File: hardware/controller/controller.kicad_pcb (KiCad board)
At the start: 4 copper layers, 100 x 70 mm, 192 parts, among them J1 USB_C_Receptacle_USB2.0_14P, J10 Conn_01x01, J11 Conn_01x01, J12 Conn_02x03_Odd_Even, J2 IDC-10, J3 XT-60, J4 Conn_01x07, J5 Conn_01x01, J6 Conn_01x01, J7 Conn_01x01, J8 Conn_02x03_Odd_Even, J9 Conn_01x01, Q1 SUD50P04-08, Q10 AOD66406, Q11 AOD66406, Q12 AOD66406, Q13 AOD66406, Q2 AOD66406, Q3 AOD66406, Q4 AOD66406, Q5 AOD66406, Q6 AOD66406, Q7 AOD66406, Q8 AOD66406, Q9 AOD66406, SW1 SW_Push, SW2 SW_Push, SW3 SW_Push, SW4 SW_SPST, U1 USBLC6-2SC6, U10 LM2105D, U11 MCP6541, U12 LM2105D, U13 MCP6541, U14 LM2105D, U15 MCP6541, U16 LM2105D, U17 MCP6541, U18 LM2105D, U19 MCP6541, U2 ESP32-C3-WROOM-02, U3 STM32U535RET6, U4 nRF24L01+ 2.4Gz Mini SMD, U5 LM1117MP-3.3, U6 LV14340, U7 MPU-6050, U8 LM2105D, U9 MCP6541, Y1 8MHz

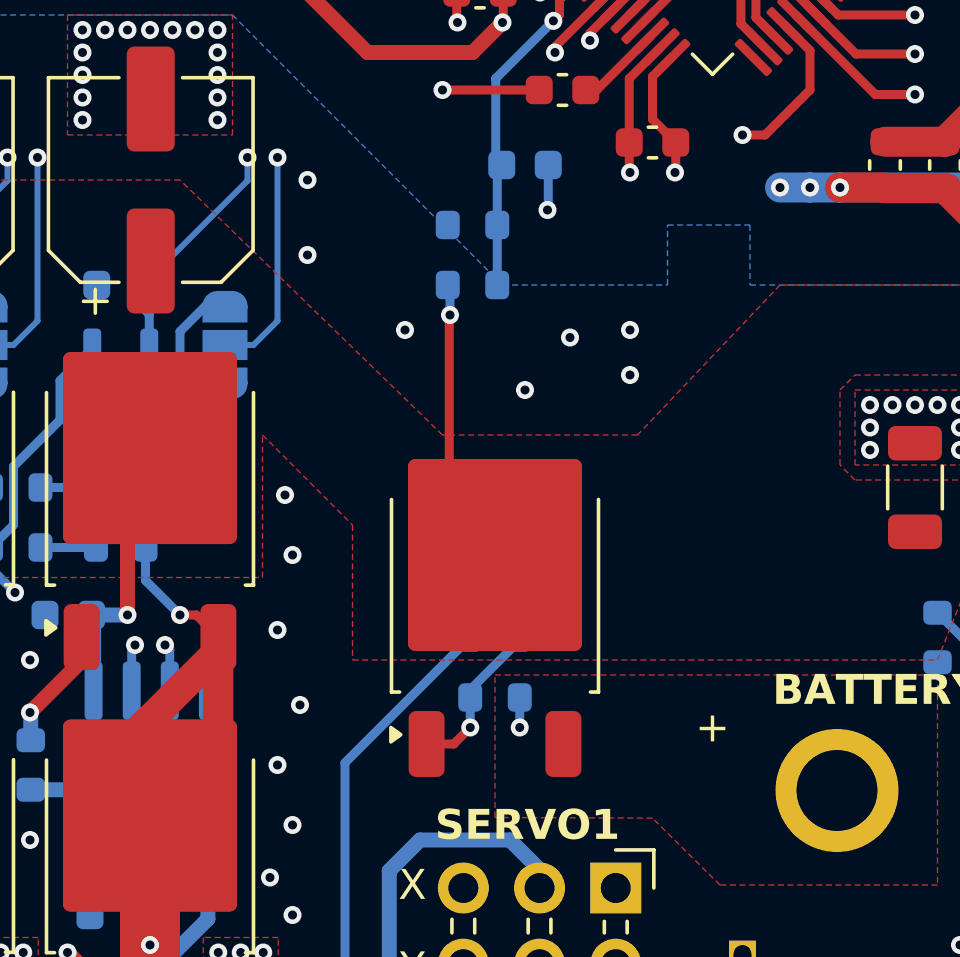
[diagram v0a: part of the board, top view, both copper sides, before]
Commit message: use diffrent P-MOSFET
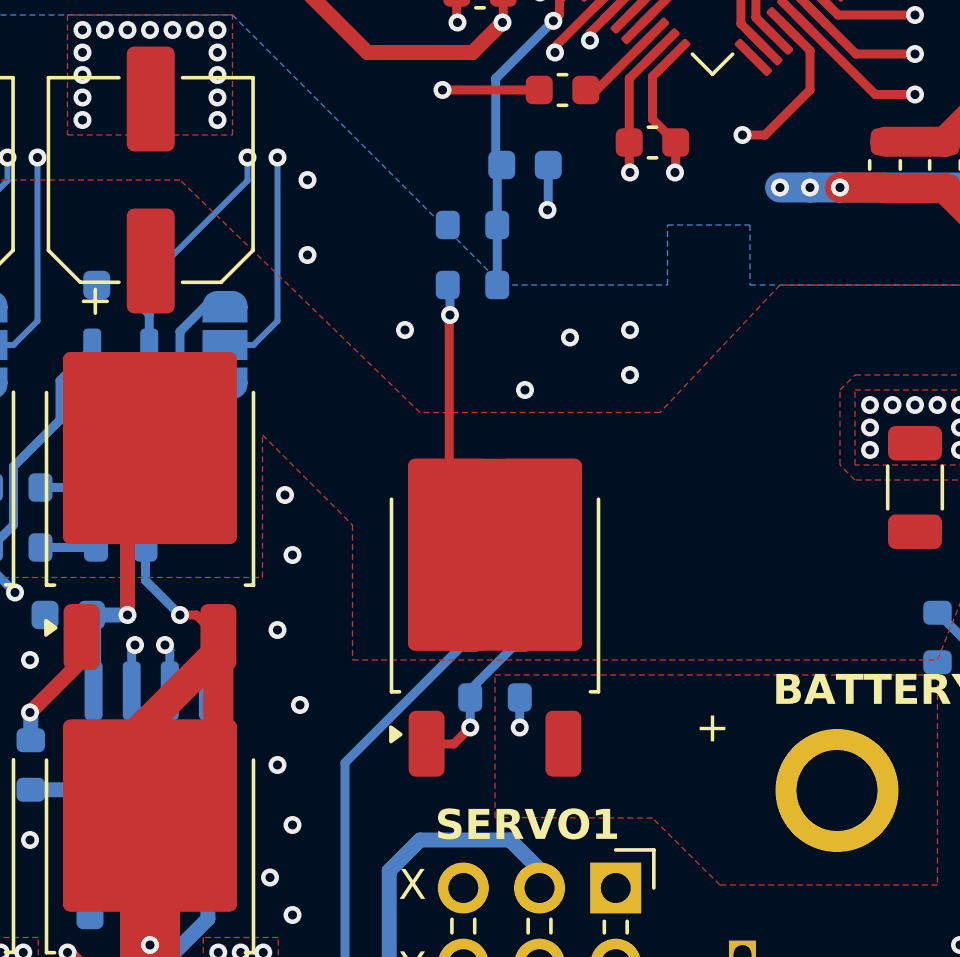
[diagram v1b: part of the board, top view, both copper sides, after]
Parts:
- Q1: value SUD50P04-08 -> AOD4189

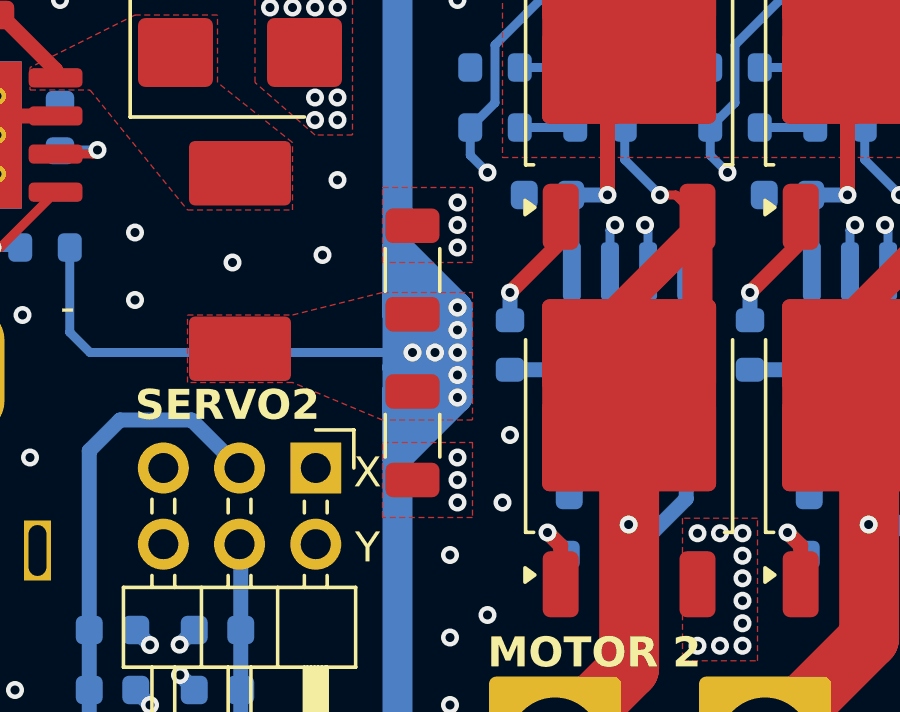
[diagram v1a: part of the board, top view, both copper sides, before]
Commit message: bigger capacitors on step down
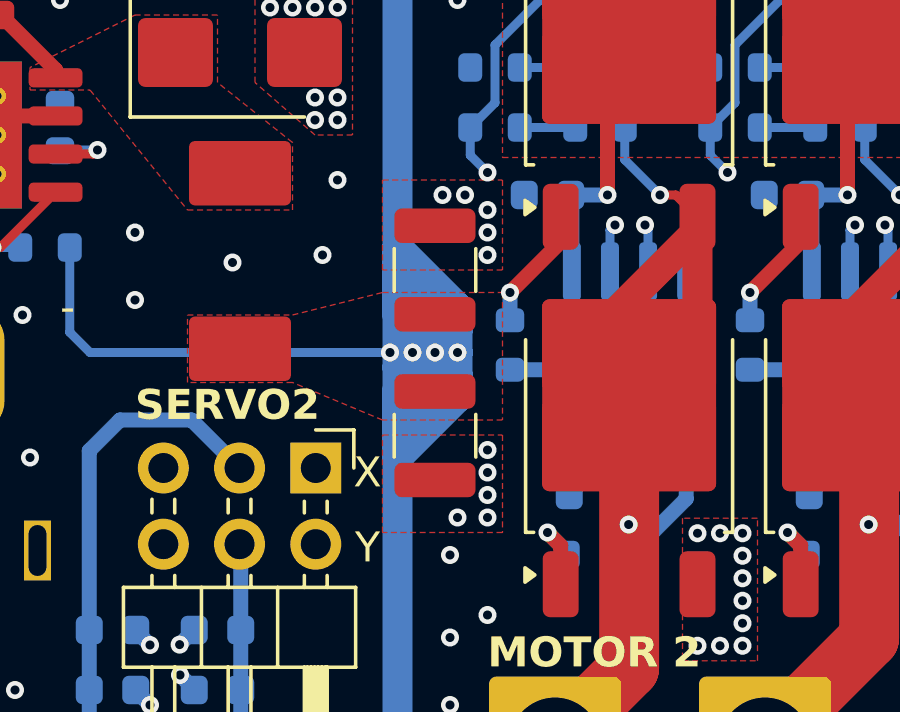
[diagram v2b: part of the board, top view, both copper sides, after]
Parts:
- C26, C27: footprint Capacitor_SMD:C_1206_3216Metric -> Capacitor_SMD:C_1210_3225Metric
- moved C26 0.75 mm to (170.0, 100.2)
- moved C27 0.75 mm to (170.0, 105.8)
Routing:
- net GND: vias 312 -> 314
- net +5V: vias 10 -> 7
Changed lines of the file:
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@@
 		)
 	)
-	(footprint "Capacitor_SMD:C_1206_3216Metric"
+	(footprint "Capacitor_SMD:C_1210_3225Metric"
 		(layer "F.Cu")
-		(at 169.25 105.775 -90)
-		(descr "Capacitor SMD 1206 (3216 Metric), square (rectangular) end terminal, IPC_7351 nominal, (Body size source: IPC-SM-782 page 76, https://www.pcb-3d.com/wordpress/wp-content/uploads/ipc-sm-782a_amendment_1_and_2.pdf), generated with kicad-footprint-generator")
+		(at 170 105.775 -90)
+		(descr "Capacitor SMD 1210 (3225 Metric), square (rectangular) end terminal, IPC_7351 nominal, (Body size source: IPC-SM-782 page 76, https://www.pcb-3d.com/wordpress/wp-content/uploads/ipc-sm-782a_amendment_1_and_2.pdf), generated with kicad-footprint-generator")
 		(tags "capacitor")
 		(property "Reference" "C27"
-			(at 0 -1.85 90)
+			(at 0 -2.3 270)
 			(layer "F.SilkS")
 			(hide yes)
@@
 		)
 		(property "Value" "47u/16V"
-			(at 0 1.85 90)
+			(at 0 2.3 -90)
 			(layer "F.Fab")
 			(effects
@@
 			)
 		)
-		(property "Footprint" "Capacitor_SMD:C_1206_3216Metric"
+		(property "Footprint" "Capacitor_SMD:C_1210_3225Metric"
 			(at 0 0 -90)
 			(unlocked yes)
@@
 		(attr smd)
 		(fp_line
-			(start -0.711252 0.91)
-			(end 0.711252 0.91)
+			(start -0.711252 1.36)
+			(end 0.711252 1.36)
 			(stroke
 				(width 0.12)
@@
 		)
 		(fp_line
-			(start -0.711252 -0.91)
-			(end 0.711252 -0.91)
+			(start -0.711252 -1.36)
+			(end 0.711252 -1.36)
 			(stroke
 				(width 0.12)
@@
 		)
 		(fp_line
-			(start -2.3 1.15)
-			(end -2.3 -1.15)
+			(start -2.3 1.6)
+			(end -2.3 -1.6)
 			(stroke
 				(width 0.05)
@@
 		)
 		(fp_line
-			(start 2.3 1.15)
-			(end -2.3 1.15)
+			(start 2.3 1.6)
+			(end -2.3 1.6)
 			(stroke
 				(width 0.05)
@@
 		)
 		(fp_line
-			(start -2.3 -1.15)
-			(end 2.3 -1.15)
+			(start -2.3 -1.6)
+			(end 2.3 -1.6)
 			(stroke
 				(width 0.05)
@@
 		)
 		(fp_line
-			(start 2.3 -1.15)
-			(end 2.3 1.15)
+			(start 2.3 -1.6)
+			(end 2.3 1.6)
 			(stroke
 				(width 0.05)
@@
 		)
 		(fp_line
-			(start -1.6 0.8)
-			(end -1.6 -0.8)
+			(start -1.6 1.25)
+			(end -1.6 -1.25)
 			(stroke
 				(width 0.1)
@@
 		)
 		(fp_line
-			(start 1.6 0.8)
-			(end -1.6 0.8)
+			(start 1.6 1.25)
+			(end -1.6 1.25)
 			(stroke
 				(width 0.1)
@@
 		)
 		(fp_line
-			(start -1.6 -0.8)
-			(end 1.6 -0.8)
+			(start -1.6 -1.25)
+			(end 1.6 -1.25)
 			(stroke
 				(width 0.1)
@@
 		)
 		(fp_line
-			(start 1.6 -0.8)
-			(end 1.6 0.8)
+			(start 1.6 -1.25)
+			(end 1.6 1.25)
 			(stroke
 				(width 0.1)
@@
 		)
 		(fp_text user "${REFERENCE}"
-			(at 0 0 90)
+			(at 0 0 -90)
 			(layer "F.Fab")
 			(effects
@@
 		(pad "1" smd roundrect
 			(at -1.475 0 270)
-			(size 1.15 1.8)
+			(size 1.15 2.7)
 			(layers "F.Cu" "F.Paste" "F.Mask")
 			(roundrect_rratio 0.217391)
@@
 		(pad "2" smd roundrect
 			(at 1.475 0 270)
-			(size 1.15 1.8)
+			(size 1.15 2.7)
 			(layers "F.Cu" "F.Paste" "F.Mask")
 			(roundrect_rratio 0.217391)
@@
 			(pintype "passive")
 		)
-		(model "${KICAD8_3DMODEL_DIR}/Capacitor_SMD.3dshapes/C_1206_3216Metric.wrl"
+		(model "${KICAD8_3DMODEL_DIR}/Capacitor_SMD.3dshapes/C_1210_3225Metric.wrl"
 			(offset
 				(xyz 0 0 0)
@@
 		)
 	)
-	(footprint "Capacitor_SMD:C_1206_3216Metric"
+	(footprint "Capacitor_SMD:C_1210_3225Metric"
 		(layer "F.Cu")
-		(at 169.25 100.25 90)
-		(descr "Capacitor SMD 1206 (3216 Metric), square (rectangular) end terminal, IPC_7351 nominal, (Body size source: IPC-SM-782 page 76, https://www.pcb-3d.com/wordpress/wp-content/uploads/ipc-sm-782a_amendment_1_and_2.pdf), generated with kicad-footprint-generator")
+		(at 170 100.25 90)
+		(descr "Capacitor SMD 1210 (3225 Metric), square (rectangular) end terminal, IPC_7351 nominal, (Body size source: IPC-SM-782 page 76, https://www.pcb-3d.com/wordpress/wp-content/uploads/ipc-sm-782a_amendment_1_and_2.pdf), generated with kicad-footprint-generator")
 		(tags "capacitor")
 		(property "Reference" "C26"
-			(at 0 -1.85 90)
+			(at 0 -2.3 90)
 			(layer "F.SilkS")
 			(hide yes)
@@
 		)
 		(property "Value" "47u/16V"
-			(at 0 1.85 90)
+			(at 0 2.3 90)
 			(layer "F.Fab")
 			(effects
@@
 			)
 		)
-		(property "Footprint" "Capacitor_SMD:C_1206_3216Metric"
+		(property "Footprint" "Capacitor_SMD:C_1210_3225Metric"
 			(at 0 0 90)
 			(unlocked yes)
@@
 		(attr smd)
 		(fp_line
-			(start -0.711252 -0.91)
-			(end 0.711252 -0.91)
+			(start -0.711252 -1.36)
+			(end 0.711252 -1.36)
 			(stroke
 				(width 0.12)
@@
 		)
 		(fp_line
-			(start -0.711252 0.91)
-			(end 0.711252 0.91)
+			(start -0.711252 1.36)
+			(end 0.711252 1.36)
 			(stroke
 				(width 0.12)
@@
 		)
 		(fp_line
-			(start 2.3 -1.15)
-			(end 2.3 1.15)
+			(start 2.3 -1.6)
+			(end 2.3 1.6)
 			(stroke
 				(width 0.05)
@@
 		)
 		(fp_line
-			(start -2.3 -1.15)
-			(end 2.3 -1.15)
+			(start -2.3 -1.6)
+			(end 2.3 -1.6)
 			(stroke
 				(width 0.05)
@@
 		)
 		(fp_line
-			(start 2.3 1.15)
-			(end -2.3 1.15)
+			(start 2.3 1.6)
+			(end -2.3 1.6)
 			(stroke
 				(width 0.05)
@@
 		)
 		(fp_line
-			(start -2.3 1.15)
-			(end -2.3 -1.15)
+			(start -2.3 1.6)
+			(end -2.3 -1.6)
 			(stroke
 				(width 0.05)
@@
 		)
 		(fp_line
-			(start 1.6 -0.8)
-			(end 1.6 0.8)
+			(start 1.6 -1.25)
+			(end 1.6 1.25)
 			(stroke
 				(width 0.1)
@@
 		)
 		(fp_line
-			(start -1.6 -0.8)
-			(end 1.6 -0.8)
+			(start -1.6 -1.25)
+			(end 1.6 -1.25)
 			(stroke
 				(width 0.1)
@@
 		)
 		(fp_line
-			(start 1.6 0.8)
-			(end -1.6 0.8)
+			(start 1.6 1.25)
+			(end -1.6 1.25)
 			(stroke
 				(width 0.1)
@@
 		)
 		(fp_line
-			(start -1.6 0.8)
-			(end -1.6 -0.8)
+			(start -1.6 1.25)
+			(end -1.6 -1.25)
 			(stroke
 				(width 0.1)
@@
 		(pad "1" smd roundrect
 			(at -1.475 0 90)
-			(size 1.15 1.8)
+			(size 1.15 2.7)
 			(layers "F.Cu" "F.Paste" "F.Mask")
 			(roundrect_rratio 0.217391)
@@
 		(pad "2" smd roundrect
 			(at 1.475 0 90)
-			(size 1.15 1.8)
+			(size 1.15 2.7)
 			(layers "F.Cu" "F.Paste" "F.Mask")
 			(roundrect_rratio 0.217391)
@@
 			(pintype "passive")
 		)
-		(model "${KICAD8_3DMODEL_DIR}/Capacitor_SMD.3dshapes/C_1206_3216Metric.wrl"
+		(model "${KICAD8_3DMODEL_DIR}/Capacitor_SMD.3dshapes/C_1210_3225Metric.wrl"
 			(offset
 				(xyz 0 0 0)
@@
 	)
 	(via
-		(at 172.25 108)
+		(at 171.75 107.75)
 		(size 0.6)
 		(drill 0.3)
@@
 	)
 	(via
-		(at 170.75 98.75)
+		(at 171.75 99)
 		(size 0.6)
 		(drill 0.3)
@@
 	)
 	(via
-		(at 172.5 105.75)
+		(at 171.75 106.25)
 		(size 0.6)
 		(drill 0.3)
@@
 	)
 	(via
-		(at 170.75 107.25)
+		(at 171.75 108.5)
 		(size 0.6)
 		(drill 0.3)
@@
 	)
 	(via
+		(at 171 97.75)
+		(size 0.6)
+		(drill 0.3)
+		(layers "F.Cu" "B.Cu")
+		(free yes)
+		(net 1)
+	)
+	(via
 		(at 186.75 79)
 		(size 0.6)
@@
 	)
 	(via
-		(at 170.75 108)
+		(at 170.75 108.5)
 		(size 0.6)
 		(drill 0.3)
@@
 	)
 	(via
-		(at 170.75 99.5)
+		(at 171.75 99.75)
 		(size 0.6)
 		(drill 0.3)
@@
 	)
 	(via
-		(at 170.75 98)
+		(at 170.25 97.75)
 		(size 0.6)
 		(drill 0.3)
@@
 	)
 	(via
-		(at 170.75 106.5)
+		(at 171.75 107)
 		(size 0.6)
 		(drill 0.3)
@@
 	)
 	(via
+		(at 171.75 98.25)
+		(size 0.6)
+		(drill 0.3)
+		(layers "F.Cu" "B.Cu")
+		(free yes)
+		(net 1)
+	)
+	(via
 		(at 183 78.25)
 		(size 0.6)
@@
 	)
 	(via
-		(at 170.75 101.5)
+		(at 168.5 103)
 		(size 0.6)
 		(drill 0.3)
@@
 	)
 	(via
-		(at 170.75 103.75)
-		(size 0.6)
-		(drill 0.3)
-		(layers "F.Cu" "B.Cu")
-		(free yes)
-		(net 13)
-	)
-	(via
 		(at 170 103)
 		(size 0.6)
@@
 	)
 	(via
-		(at 170.75 102.25)
-		(size 0.6)
-		(drill 0.3)
-		(layers "F.Cu" "B.Cu")
-		(free yes)
-		(net 13)
-	)
-	(via
 		(at 144.5 83.5)
 		(size 0.6)
@@
 		(net 13)
 	)
-	(via
-		(at 170.75 104.5)
-		(size 0.6)
-		(drill 0.3)
-		(layers "F.Cu" "B.Cu")
-		(free yes)
-		(net 13)
-	)
 	(segment
 		(start 136.525 114.25)
@@
 		(polygon
 			(pts
-				(xy 171.25 97.5) (xy 171.25 100) (xy 168.25 100) (xy 168.25 97.5)
+				(xy 172.25 97.25) (xy 172.25 100.25) (xy 168.25 100.25) (xy 168.25 97.25)
 			)
 		)
@@
 		(polygon
 			(pts
-				(xy 165.25 101.75) (xy 168.25 101) (xy 171.25 101) (xy 171.25 105.25) (xy 168.25 105.25) (xy 165.25 104)
+				(xy 165.25 101.75) (xy 168.25 101) (xy 172.25 101) (xy 172.25 105.25) (xy 168.25 105.25) (xy 165.25 104)
 				(xy 161.75 104) (xy 161.75 101.75)
 			)
@@
 		(polygon
 			(pts
-				(xy 168.25 108.5) (xy 168.25 106) (xy 171.25 106) (xy 171.25 108.5)
+				(xy 168.25 109) (xy 168.25 105.75) (xy 172.25 105.75) (xy 172.25 109)
 			)
 		)

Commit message: wip
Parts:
- removed the SW2 at (151.5, 56.0)
- removed SW3: SW_Push, hogger2:spst_6x3mm
- removed the U3 at (142.2, 72.5)
- added J13: Conn_01x06, Connector_PinHeader_2.54mm:PinHeader_1x06_P2.54mm_Vertical, F.Cu at (300.7, 82.4)
- added J14: Conn_01x03, Connector_PinHeader_2.54mm:PinHeader_1x03_P2.54mm_Vertical, F.Cu at (296.0, 71.3)
- added J15: Mini-SPOX, hogger2:Molex-MiniSPOX-22057035-5268, F.Cu at (137.0, 129.4)
- added J16: Mini-SPOX, hogger2:Molex-MiniSPOX-22057035-5268, F.Cu at (169.5, 128.9)
- added R50: 220k, Resistor_SMD:R_0603_1608Metric, F.Cu at (282.5, 61.3)
- added R51: 10k, Resistor_SMD:R_0603_1608Metric, F.Cu at (282.5, 63.8)
- added R52: 220k, Resistor_SMD:R_0603_1608Metric, F.Cu at (282.5, 66.3)
- added R53: 68, Resistor_SMD:R_0603_1608Metric, F.Cu at (282.5, 68.8)
- added R54: 220k, Resistor_SMD:R_0603_1608Metric, F.Cu at (282.5, 71.3)
- added R55: 47k, Resistor_SMD:R_0603_1608Metric, F.Cu at (282.5, 73.8)
- added R56: 68, Resistor_SMD:R_0603_1608Metric, F.Cu at (282.5, 76.3)
- added R57: 47k, Resistor_SMD:R_0603_1608Metric, F.Cu at (282.5, 78.9)
- added R58: 47k, Resistor_SMD:R_0603_1608Metric, F.Cu at (286.6, 58.8)
- added R59: 10k, Resistor_SMD:R_0603_1608Metric, F.Cu at (286.6, 61.3)
- added R60: 68, Resistor_SMD:R_0603_1608Metric, F.Cu at (286.6, 63.8)
- added R61: 47k, Resistor_SMD:R_0603_1608Metric, F.Cu at (286.6, 66.3)
- added R62: 68, Resistor_SMD:R_0603_1608Metric, F.Cu at (286.6, 68.8)
- added R63: 47k, Resistor_SMD:R_0603_1608Metric, F.Cu at (286.6, 71.3)
- added U2: STM32H523RETx, Package_QFP:LQFP-64_10x10mm_P0.5mm, F.Cu at (150.0, 71.5)
- added U20: TXS0101DBV, Package_TO_SOT_SMD:SOT-23-6, F.Cu at (294.3, 127.4)
- added U21: TXS0101DBV, Package_TO_SOT_SMD:SOT-23-6, F.Cu at (294.3, 132.0)
- C1: value 10u -> 4.7u
- C10, C11: value 100n -> 100u; footprint Capacitor_SMD:C_0603_1608Metric -> Capacitor_SMD:C_1206_3216Metric
- C12: value 100n -> 100u; footprint Capacitor_SMD:C_0603_1608Metric -> Capacitor_SMD:C_1206_3216Metric; moved to F.Cu
- C13, C14: value 22p -> 100u; footprint Capacitor_SMD:C_0603_1608Metric -> Capacitor_SMD:C_1206_3216Metric
- C15, C41, C45, C55, C62, C65, C66, C67, C76, JP1, JP2, JP3, JP4, JP5, JP6, R1, R10, R12, R13, R14, R15, R16, R17, R18, R19, R2, R27, R36, R4, R42, R5, R6, R8, R9: moved to F.Cu
- C16: value 100n -> 22p; moved to F.Cu
- C17: value 10u -> 22p; moved to F.Cu
- C18: value 4.7u -> 2.2u
- C19: value 100n -> 2.2u; moved to F.Cu
- C20: value 100n/16V -> 100n
- C21: value 100n -> 100n/16V
- C22: value 4.7u -> 100n
- C24: value 100n -> 4.7u
- C25: value 10u/50V -> 100n; footprint Capacitor_SMD:C_1206_3216Metric -> Capacitor_SMD:C_0603_1608Metric
- C26: value 47u/16V -> 10u/50V; footprint Capacitor_SMD:C_1210_3225Metric -> Capacitor_SMD:C_1206_3216Metric
- C28: value 22n -> 47u/16V; footprint Capacitor_SMD:C_0603_1608Metric -> Capacitor_SMD:C_1210_3225Metric; moved to F.Cu
- C29: value 100n -> 22n
- C31: value 10u -> 100n
- C32: value 100n -> 10u
- C34: value 2n2 -> 100n
- C35: value 1u/50V -> 2n2; moved to F.Cu
- C36: value 100n/50V -> 100n; moved to F.Cu
- C37: value 100n -> 220n; moved to F.Cu
- C38: value 47u/50V -> 4.7u; footprint Capacitor_SMD:CP_Elec_6.3x7.7 -> Capacitor_SMD:C_0603_1608Metric
- C39, C60: value 1n -> 1u/50V; moved to F.Cu
- C40: value 1u/50V -> 100n; moved to F.Cu
- C42, C50: value 100n -> 1n; moved to F.Cu
- C44, C49, C70: value 1n -> 100n; moved to F.Cu
- C46, C57: value 100n/50V -> 1n; moved to F.Cu
- C47: value 100n -> 100n/50V; moved to F.Cu
- C51, C54: value 10u -> 1u/50V; moved to F.Cu
- C52: value 10u -> 100n/50V; moved to F.Cu
- C53, C75: value 10u -> 47u/50V; footprint Capacitor_SMD:C_0603_1608Metric -> Capacitor_SMD:CP_Elec_6.3x7.7; moved to F.Cu
- C56: value 1u/50V -> 100n/50V; moved to F.Cu
- C58, C63, C68, C71: value 100n -> 47u/50V; footprint Capacitor_SMD:C_0603_1608Metric -> Capacitor_SMD:CP_Elec_6.3x7.7; moved to F.Cu
- C59, C64, C69: value 47u/50V -> 100n; footprint Capacitor_SMD:CP_Elec_6.3x7.7 -> Capacitor_SMD:C_0603_1608Metric
- C6: value 1u -> 100n
- C61: value 1u/50V -> 1n; moved to F.Cu
- C7: value 1u -> 100n; moved to F.Cu
- C72, C73, C74: value 10u -> 100n; moved to F.Cu
- C8: value 10u -> 1u
- J12: value Conn_02x03_Odd_Even -> Conn_01x01; footprint Connector_PinHeader_2.54mm:PinHeader_2x03_P2.54mm_Horizontal -> Connector_Wire:SolderWire-2.5sqmm_1x01_D2.4mm_OD4.4mm
- J8: value Conn_02x03_Odd_Even -> Conn_01x06; footprint Connector_PinHeader_2.54mm:PinHeader_2x03_P2.54mm_Horizontal -> Connector_PinHeader_2.54mm:PinHeader_1x06_P2.54mm_Vertical
- J9: value Conn_01x01 -> Conn_01x03; footprint Connector_Wire:SolderWire-2.5sqmm_1x01_D2.4mm_OD4.4mm -> Connector_PinHeader_2.54mm:PinHeader_1x03_P2.54mm_Vertical
- R11: value 51k -> 47k; moved to F.Cu
- R20: value 100 -> 4.7k; moved to F.Cu
- R21: value 47k -> 4.7k; moved to F.Cu
- R22, R28, R37, R43, R48: value 10k -> 47k; moved to F.Cu
- R23, R35, R44: value 100 -> 68; moved to F.Cu
- R24, R30, R45: value 47k -> 10k; moved to F.Cu
- R25, R34, R40, R46, R49: value 100 -> 47k; moved to F.Cu
- R26, R32, R39, R41, R47: value 47k -> 68; moved to F.Cu
- R29, R31: value 100 -> 220k; moved to F.Cu
- R3: value 10k -> 1k; moved to F.Cu
- R33: value 10k -> 220k; moved to F.Cu
- R38: value 100 -> 10k; moved to F.Cu
- R7: value 1k -> 10k; moved to F.Cu
- U10, U12, U14, U16, U18, U8: value LM2105D -> MCP6541; footprint Package_SO:SOIC-8_3.9x4.9mm_P1.27mm -> Package_TO_SOT_SMD:SOT-23-5; moved to F.Cu
- U11, U13, U15, U17, U19, U9: value MCP6541 -> LM2105D; footprint Package_TO_SOT_SMD:SOT-23-5 -> Package_SO:SOIC-8_3.9x4.9mm_P1.27mm; moved to F.Cu
- U4: value nRF24L01+ 2.4Gz Mini SMD -> LM1117MP-3.3; footprint hogger2:nRF24L01p_Mini_SMD -> Package_TO_SOT_SMD:SOT-223-3_TabPin2; moved to F.Cu
- U5: value LM1117MP-3.3 -> LV14340; footprint Package_TO_SOT_SMD:SOT-223-3_TabPin2 -> hogger2:LV14340
- U6: value LV14340 -> MPU-6050; footprint hogger2:LV14340 -> hogger2:MPU6050_handsolder
- U7: value MPU-6050 -> HMC5883L; footprint hogger2:MPU6050_handsolder -> hogger2:HMC5883L_handsolder
- moved U7 195.5 mm to (295.2, 147.8), turned to 0 degrees
- moved C31 193.8 mm to (281.7, 140.0), turned to 0 degrees
- moved C32 193.0 mm to (281.7, 142.5), turned to 0 degrees
- moved R20 189.9 mm to (289.7, 140.0), turned to 0 degrees
- moved R21 189.1 mm to (289.7, 142.5), turned to 0 degrees
- moved C38 188.6 mm to (285.7, 145.0), turned to 0 degrees
- moved C37 187.7 mm to (285.7, 142.5)
- moved C33 187.6 mm to (281.7, 145.0), turned to 0 degrees
- moved C35 185.2 mm to (285.7, 137.5)
- moved R18 182.3 mm to (285.7, 147.5), turned to 0 degrees
- moved C36 182.3 mm to (285.7, 140.0)
- moved R19 181.1 mm to (289.7, 137.5), turned to 0 degrees
- moved C30 179.3 mm to (281.7, 137.5), turned to 0 degrees
- moved C34 178.1 mm to (281.7, 147.5), turned to 0 degrees
- moved C54 152.7 mm to (274.5, 58.8)
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- renumbered SW4 to SW2, U2 to U3
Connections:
- C12 pad 1: /microcontroller/STM_RESET -> +3.3V
- C13 pad 1: /microcontroller/STM_OSC_IN -> +3.3V
- C14 pad 1: /microcontroller/STM_OSC_OUT -> +3.3V
- C15 pad 1: /microcontroller/ESP_BOOT -> +3.3V
- C16 pad 1: +3.3V -> /microcontroller/STM_OSC_IN
- C17 pad 1: +3.3V -> /microcontroller/STM_OSC_OUT
- C19 pad 1: VBUS_SENSE -> /microcontroller/STM_VCAP
- C20 pad 1: Net-(U6-BOOT) -> VBUS_SENSE
- C20 pad 2: Net-(D3-K) -> GND
- C21 pad 1: +5V -> Net-(U5-BOOT)
- C21 pad 2: GND -> Net-(D3-K)
- C23 pad 1: +3.3V -> +5V
- C25 pad 1: VBUS -> +3.3V
- C26 pad 1: +5V -> VBUS
- C28 pad 1: Net-(U6-SS) -> +5V
- C29 pad 1: +3.3V -> Net-(U5-SS)
- C33 pad 1: /sensors/IMU_REGOUT -> +3.3V
- C34 pad 1: /sensors/IMU_CPOUT -> /sensors/IMU_REGOUT
- C35 pad 1: GND -> /sensors/IMU_CPOUT
- C35 pad 2: VBUS -> GND
- C36 pad 1: Net-(U8-BST) -> +3.3V
- C36 pad 2: /hog1/PHASE_U -> GND
- C37 pad 1: GND -> /sensors/MAG_SETP
- C37 pad 2: +3.3V -> /sensors/MAG_SETC
- C38 pad 1: VBUS -> /sensors/MAG_C1
- C39 pad 1: /hog1/BEMF_U -> GND
- C39 pad 2: GND -> VBUS
- C40 pad 2: VBUS -> +3.3V
- C41 pad 1: Net-(U10-BST) -> Net-(U9-BST)
- C41 pad 2: /hog1/PHASE_V -> /motor1/PHASE_U
- C42 pad 1: GND -> /motor1/BEMF_U
- C42 pad 2: +3.3V -> GND
- C44 pad 1: /hog1/BEMF_V -> GND
- C44 pad 2: GND -> +3.3V
- C46 pad 1: Net-(U12-BST) -> /motor1/BEMF_V
- C46 pad 2: /hog1/PHASE_W -> GND
- C47 pad 1: GND -> Net-(U11-BST)
- C47 pad 2: +3.3V -> /motor1/PHASE_V
- C49 pad 1: /hog1/BEMF_W -> GND
- C49 pad 2: GND -> +3.3V
- C50 pad 1: +5V -> /motor1/BEMF_W
- C51 pad 1: +5V -> GND
- C51 pad 2: GND -> VBUS
- C52 pad 1: +5V -> Net-(U13-BST)
- C52 pad 2: GND -> /motor1/PHASE_W
- C53 pad 1: +5V -> VBUS
- C54 pad 1: +5V -> GND
- C54 pad 2: GND -> VBUS
- C55 pad 1: +5V -> GND
- C55 pad 2: GND -> +3.3V
- C56 pad 1: GND -> Net-(U15-BST)
- C56 pad 2: VBUS -> /motor2/PHASE_U
- C57 pad 1: Net-(U14-BST) -> /motor2/BEMF_U
- C57 pad 2: /hog2/PHASE_U -> GND
- C58 pad 1: GND -> VBUS
- C58 pad 2: +3.3V -> GND
- C59 pad 1: VBUS -> GND
- C59 pad 2: GND -> +3.3V
- C60 pad 1: /hog2/BEMF_U -> GND
- C60 pad 2: GND -> VBUS
- C61 pad 1: GND -> /motor2/BEMF_V
- C61 pad 2: VBUS -> GND
- C62 pad 1: Net-(U16-BST) -> Net-(U17-BST)
- C62 pad 2: /hog2/PHASE_V -> /motor2/PHASE_V
- C63 pad 1: GND -> VBUS
- C63 pad 2: +3.3V -> GND
- C64 pad 1: VBUS -> GND
- C64 pad 2: GND -> +3.3V
- C65 pad 1: /hog2/BEMF_V -> /motor2/BEMF_W
- C67 pad 1: Net-(U18-BST) -> Net-(U19-BST)
- C67 pad 2: /hog2/PHASE_W -> /motor2/PHASE_W
- C68 pad 1: GND -> VBUS
- C68 pad 2: +3.3V -> GND
- C69 pad 1: VBUS -> +3.3V
- C7 pad 1: /microcontroller/ESP_EN -> +3.3V
- C70 pad 1: /hog2/BEMF_W -> +5V
- C71 pad 1: +5V -> VBUS
- C72 pad 1: +5V -> VBUS
- C73 pad 1: +5V -> +3.3V
- C75 pad 1: +5V -> VBUS
- C76 pad 1: +5V -> VBUS
- C9 pad 1: +3.3V -> /microcontroller/STM_RESET
- H1 pad 1: GND -> unconnected-(H1-Pad1)_1
- H2 pad 1: GND -> unconnected-(H2-Pad1)_4
- H3 pad 1: GND -> unconnected-(H3-Pad1)
- H4 pad 1: GND -> unconnected-(H4-Pad1)_2
- J1 pad A4: /microcontroller/ESP_USB_VBUS -> +5V
- J1 pad A9: /microcontroller/ESP_USB_VBUS -> +5V
- J1 pad B4: /microcontroller/ESP_USB_VBUS -> +5V
- J1 pad B9: /microcontroller/ESP_USB_VBUS -> +5V
- J10 pad 1: /hog2/PHASE_V -> /motor2/PHASE_U
- J11 pad 1: /hog2/PHASE_W -> /motor2/PHASE_V
- J12 pad 1: SERVO2_PWM_X -> /motor2/PHASE_W
- J2 pad 3: /microcontroller/STM_SWO -> unconnected-(J2-Pin_3-Pad3)
- J5 pad 1: /hog1/PHASE_U -> /motor1/PHASE_U
- J6 pad 1: /hog1/PHASE_V -> /motor1/PHASE_V
- J7 pad 1: /hog1/PHASE_W -> /motor1/PHASE_W
- J8 pad 1: SERVO1_PWM_X -> MOTOR1_PWM_UH
- J8 pad 2: SERVO1_PWM_Y -> MOTOR1_PWM_UL
- J8 pad 3: +5V -> MOTOR1_PWM_VH
- J8 pad 4: +5V -> MOTOR1_PWM_VL
- J8 pad 5: GND -> MOTOR1_PWM_WH
- J8 pad 6: GND -> MOTOR1_PWM_WL
- J9 pad 1: /hog2/PHASE_U -> MOTOR1_BEMF_U
- JP1 pad 1: /hog1/BEMF_U -> Net-(JP1-A)
- JP1 pad 3: Net-(JP1-B) -> /motor1/BEMF_U
- JP2 pad 1: /hog1/BEMF_V -> Net-(JP2-A)
- JP2 pad 3: Net-(JP2-B) -> /motor1/BEMF_V
- JP3 pad 1: /hog1/BEMF_W -> Net-(JP3-A)
- JP3 pad 3: Net-(JP3-B) -> /motor1/BEMF_W
- JP4 pad 1: /hog2/BEMF_U -> Net-(JP4-A)
- JP4 pad 3: Net-(JP4-B) -> /motor2/BEMF_U
- JP5 pad 1: /hog2/BEMF_V -> Net-(JP5-A)
- JP5 pad 3: Net-(JP5-B) -> /motor2/BEMF_V
- JP6 pad 1: /hog2/BEMF_W -> Net-(JP6-A)
- JP6 pad 3: Net-(JP6-B) -> /motor2/BEMF_W
- Q10 pad 3: /hog2/PHASE_V -> /motor2/PHASE_V
- Q11 pad 2: /hog2/PHASE_V -> /motor2/PHASE_V
- Q12 pad 3: /hog2/PHASE_W -> /motor2/PHASE_W
- Q13 pad 2: /hog2/PHASE_W -> /motor2/PHASE_W
- Q2 pad 3: /hog1/PHASE_U -> /motor1/PHASE_U
- Q3 pad 2: /hog1/PHASE_U -> /motor1/PHASE_U
- Q4 pad 3: /hog1/PHASE_V -> /motor1/PHASE_V
- Q5 pad 2: /hog1/PHASE_V -> /motor1/PHASE_V
- Q6 pad 3: /hog1/PHASE_W -> /motor1/PHASE_W
- Q7 pad 2: /hog1/PHASE_W -> /motor1/PHASE_W
- Q8 pad 3: /hog2/PHASE_U -> /motor2/PHASE_U
- Q9 pad 2: /hog2/PHASE_U -> /motor2/PHASE_U
- R14 pad 2: Net-(U6-FB) -> Net-(U5-FB)
- R15 pad 1: Net-(U6-RT/SYNC) -> Net-(U5-RT/SYNC)
- R16 pad 1: Net-(U6-FB) -> Net-(U5-FB)
- R20 pad 1: Net-(U8-GH) -> +3.3V
- R20 pad 2: Net-(Q2-G) -> MAG_SDA
- R21 pad 1: /hog1/PHASE_U -> +3.3V
- R21 pad 2: /hog1/BEMF_U -> MAG_SCL
- R22 pad 1: /hog1/BEMF_U -> /motor1/PHASE_U
- R22 pad 2: GND -> /motor1/BEMF_U
- R23 pad 1: Net-(U8-GL) -> Net-(U9-GH)
- R23 pad 2: Net-(Q3-G) -> Net-(Q2-G)
- R24 pad 1: /hog1/BEMF_U -> /motor1/BEMF_U
- R24 pad 2: /hog1/BEMF_ZERO -> GND
- R25 pad 1: Net-(U10-GH) -> Net-(Q2-G)
- R25 pad 2: Net-(Q4-G) -> /motor1/PHASE_U
- R26 pad 1: /hog1/PHASE_V -> Net-(U9-GL)
- R26 pad 2: /hog1/BEMF_V -> Net-(Q3-G)
- R27 pad 1: /hog1/BEMF_V -> Net-(Q3-G)
- R27 pad 2: /hog1/BEMF_ZERO -> GND
- R28 pad 1: /hog1/BEMF_V -> /motor1/PHASE_V
- R28 pad 2: GND -> /motor1/BEMF_V
- R29 pad 1: Net-(U10-GL) -> /motor1/BEMF_U
- R29 pad 2: Net-(Q5-G) -> /motor1/BEMF_ZERO
- R3 pad 1: +3.3V -> /microcontroller/ESP_LED
- R3 pad 2: /microcontroller/ESP_EN -> Net-(D1-A)
- R30 pad 1: /hog1/BEMF_W -> /motor1/BEMF_V
- R30 pad 2: /hog1/BEMF_ZERO -> GND
- R31 pad 1: Net-(U12-GH) -> /motor1/BEMF_V
- R31 pad 2: Net-(Q6-G) -> /motor1/BEMF_ZERO
- R32 pad 1: /hog1/PHASE_W -> Net-(U11-GH)
- R32 pad 2: /hog1/BEMF_W -> Net-(Q4-G)
- R33 pad 1: /hog1/BEMF_W -> /motor1/BEMF_W
- R33 pad 2: GND -> /motor1/BEMF_ZERO
- R34 pad 1: Net-(U12-GL) -> Net-(Q4-G)
- R34 pad 2: Net-(Q7-G) -> /motor1/PHASE_V
- R35 pad 1: Net-(U14-GH) -> Net-(U11-GL)
- R35 pad 2: Net-(Q8-G) -> Net-(Q5-G)
- R36 pad 1: /hog2/PHASE_U -> Net-(Q5-G)
- R36 pad 2: /hog2/BEMF_U -> GND
- R37 pad 1: /hog2/BEMF_U -> /motor1/PHASE_W
- R37 pad 2: GND -> /motor1/BEMF_W
- R38 pad 1: Net-(U14-GL) -> /motor1/BEMF_W
- R38 pad 2: Net-(Q9-G) -> GND
- R39 pad 1: /hog2/BEMF_U -> Net-(U13-GH)
- R39 pad 2: /hog2/BEMF_ZERO -> Net-(Q6-G)
- R40 pad 1: Net-(U16-GH) -> Net-(Q6-G)
- R40 pad 2: Net-(Q10-G) -> /motor1/PHASE_W
- R41 pad 1: /hog2/PHASE_V -> Net-(U13-GL)
- R41 pad 2: /hog2/BEMF_V -> Net-(Q7-G)
- R42 pad 1: /hog2/BEMF_V -> Net-(Q7-G)
- R42 pad 2: /hog2/BEMF_ZERO -> GND
- R43 pad 1: /hog2/BEMF_V -> /motor2/PHASE_U
- R43 pad 2: GND -> /motor2/BEMF_U
- R44 pad 1: Net-(U16-GL) -> Net-(U15-GH)
- R44 pad 2: Net-(Q11-G) -> Net-(Q8-G)
- R45 pad 1: /hog2/BEMF_W -> /motor2/BEMF_U
- R45 pad 2: /hog2/BEMF_ZERO -> GND
- R46 pad 1: Net-(U18-GH) -> Net-(Q8-G)
- R46 pad 2: Net-(Q12-G) -> /motor2/PHASE_U
- R47 pad 1: /hog2/PHASE_W -> Net-(U15-GL)
- R47 pad 2: /hog2/BEMF_W -> Net-(Q9-G)
- R48 pad 1: /hog2/BEMF_W -> Net-(Q9-G)
- R49 pad 1: Net-(U18-GL) -> /motor2/PHASE_V
- R49 pad 2: Net-(Q13-G) -> /motor2/BEMF_V
- R5 pad 2: /microcontroller/ESP_IO8 -> /microcontroller/ESP_BOOT
- R6 pad 2: /microcontroller/ESP_IO2 -> /microcontroller/ESP_IO8
- R7 pad 1: /microcontroller/ESP_LED -> +3.3V
- R7 pad 2: Net-(D1-A) -> /microcontroller/ESP_IO2
- R8 pad 2: /microcontroller/ESP_BOOT -> /microcontroller/ESP_EN
- SW1 pad 2: /microcontroller/ESP_EN -> /microcontroller/STM_RESET
- U1 pad 5: /microcontroller/ESP_USB_VBUS -> +5V
- U10 pad 1: VBUS -> Net-(JP2-A)
- U10 pad 2: MOTOR1_PWM_VH -> GND
- U10 pad 3: MOTOR1_PWM_VL -> /motor1/BEMF_V
- U10 pad 4: GND -> /motor1/BEMF_ZERO
- U10 pad 5: Net-(U10-GL) -> +3.3V
- U11 pad 1: Net-(JP2-B) -> VBUS
- U11 pad 2: GND -> MOTOR1_PWM_VH
- U11 pad 3: /hog1/BEMF_V -> MOTOR1_PWM_VL
- U11 pad 4: /hog1/BEMF_ZERO -> GND
- U11 pad 5: +3.3V -> Net-(U11-GL)
- U12 pad 1: VBUS -> Net-(JP3-A)
- U12 pad 2: MOTOR1_PWM_WH -> GND
- U12 pad 3: MOTOR1_PWM_WL -> /motor1/BEMF_W
- U12 pad 4: GND -> /motor1/BEMF_ZERO
- U12 pad 5: Net-(U12-GL) -> +3.3V
- U13 pad 1: Net-(JP3-B) -> VBUS
- U13 pad 2: GND -> MOTOR1_PWM_WH
- U13 pad 3: /hog1/BEMF_W -> MOTOR1_PWM_WL
- U13 pad 4: /hog1/BEMF_ZERO -> GND
- U13 pad 5: +3.3V -> Net-(U13-GL)
- U14 pad 1: VBUS -> Net-(JP4-A)
- U14 pad 2: MOTOR2_PWM_UH -> GND
- U14 pad 3: MOTOR2_PWM_UL -> /motor2/BEMF_U
- U14 pad 4: GND -> /motor2/BEMF_ZERO
- U14 pad 5: Net-(U14-GL) -> +3.3V
- U15 pad 1: Net-(JP4-B) -> VBUS
- U15 pad 2: GND -> MOTOR2_PWM_UH
- U15 pad 3: /hog2/BEMF_U -> MOTOR2_PWM_UL
- U15 pad 4: /hog2/BEMF_ZERO -> GND
- U15 pad 5: +3.3V -> Net-(U15-GL)
- U16 pad 1: VBUS -> Net-(JP5-A)
- U16 pad 2: MOTOR2_PWM_VH -> GND
- U16 pad 3: MOTOR2_PWM_VL -> /motor2/BEMF_V
- U16 pad 4: GND -> /motor2/BEMF_ZERO
- U16 pad 5: Net-(U16-GL) -> +3.3V
- U17 pad 1: Net-(JP5-B) -> VBUS
- U17 pad 2: GND -> MOTOR2_PWM_VH
- U17 pad 3: /hog2/BEMF_V -> MOTOR2_PWM_VL
- U17 pad 4: /hog2/BEMF_ZERO -> GND
- U17 pad 5: +3.3V -> Net-(U17-GL)
- U18 pad 1: VBUS -> Net-(JP6-A)
- U18 pad 2: MOTOR2_PWM_WH -> GND
- U18 pad 3: MOTOR2_PWM_WL -> /motor2/BEMF_W
- U18 pad 4: GND -> /motor2/BEMF_ZERO
- U18 pad 5: Net-(U18-GL) -> +3.3V
- U19 pad 1: Net-(JP6-B) -> VBUS
- U19 pad 2: GND -> MOTOR2_PWM_WH
- U19 pad 3: /hog2/BEMF_W -> MOTOR2_PWM_WL
- U19 pad 4: /hog2/BEMF_ZERO -> GND
- U19 pad 5: +3.3V -> Net-(U19-GL)
- U3 pad 10: /microcontroller/ESP_LED -> /microcontroller/ESP_RDY
- U3 pad 15: VBUS_SENSE -> /microcontroller/ESP_HANDSHAKE
- U3 pad 18: unconnected-(U2-IO0-Pad18) -> /microcontroller/ESP_LED
- U3 pad 3: unconnected-(U2-IO4-Pad3) -> /microcontroller/ESP_MOSI
- U3 pad 4: unconnected-(U2-IO5-Pad4) -> /microcontroller/ESP_MISO
- U3 pad 5: unconnected-(U2-IO6-Pad5) -> /microcontroller/ESP_SCK
- U3 pad 6: unconnected-(U2-IO7-Pad6) -> /microcontroller/ESP_CS
- U4 pad 1: +3.3V -> GND
- U4 pad 2: GND -> +3.3V
- U4 pad 3: /microcontroller/NRF_CE -> +5V
- U5 pad 1: GND -> Net-(U5-BOOT)
- U5 pad 2: +3.3V -> VBUS
- U5 pad 3: +5V -> unconnected-(U5-EN-Pad3)
- U6 pad 1: Net-(U6-BOOT) -> GND
- U6 pad 2: VBUS -> unconnected-(U6-NC-Pad2)
- U6 pad 4: Net-(U6-RT/SYNC) -> unconnected-(U6-NC-Pad4)
- U6 pad 5: Net-(U6-FB) -> unconnected-(U6-NC-Pad5)
- U6 pad 6: Net-(U6-SS) -> unconnected-(U6-AUX_DA-Pad6)
- U6 pad 7: GND -> unconnected-(U6-AUX_CL-Pad7)
- U6 pad 8: Net-(D3-K) -> +3.3V
- U7 pad 1: GND -> MAG_SCL
- U7 pad 10: /sensors/IMU_REGOUT -> /sensors/MAG_C1
- U7 pad 12: IMU_INT -> /sensors/MAG_SETC
- U7 pad 14: unconnected-(U7-NC-Pad14) -> (no net)
- U7 pad 15: unconnected-(U7-NC-Pad15) -> MAG_INT
- U7 pad 16: unconnected-(U7-NC-Pad16) -> MAG_SDA
- U7 pad 2: unconnected-(U7-NC-Pad2) -> +3.3V
- U7 pad 3: unconnected-(U7-NC-Pad3) -> (no net)
- U7 pad 4: unconnected-(U7-NC-Pad4) -> +3.3V
- U7 pad 5: unconnected-(U7-NC-Pad5) -> (no net)
- U7 pad 6: unconnected-(U7-AUX_DA-Pad6) -> (no net)
- U7 pad 7: unconnected-(U7-AUX_CL-Pad7) -> (no net)
- U7 pad 8: +3.3V -> /sensors/MAG_SETP
- U8 pad 1: VBUS -> Net-(JP1-A)
- U8 pad 2: MOTOR1_PWM_UH -> GND
- U8 pad 3: MOTOR1_PWM_UL -> /motor1/BEMF_U
- U8 pad 4: GND -> /motor1/BEMF_ZERO
- U8 pad 5: Net-(U8-GL) -> +3.3V
- U9 pad 1: Net-(JP1-B) -> VBUS
- U9 pad 2: GND -> MOTOR1_PWM_UH
- U9 pad 3: /hog1/BEMF_U -> MOTOR1_PWM_UL
- U9 pad 4: /hog1/BEMF_ZERO -> GND
- U9 pad 5: +3.3V -> Net-(U9-GL)
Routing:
- net +5V: track 205.3 -> 0.00 mm, vias 7 -> 0
- net +3.3V: track 187.8 -> 0.00 mm, vias 38 -> 0
- net GND: track 130.0 -> 0.00 mm, vias 314 -> 0
- net Net-(SW2-A): track 100.2 -> 0.00 mm, vias 1 -> 0
- net SERVO2_PWM_X: track 87.4 -> 0.00 mm, vias 1 -> 0
- net SERVO2_PWM_Y: track 78.1 -> 0.00 mm, vias 1 -> 0
- net MOTOR2_BEMF_W: track 72.2 -> 0.00 mm, vias 2 -> 0
- net MOTOR2_PWM_WL: track 69.1 -> 0.00 mm, vias 2 -> 0
- net MOTOR2_BEMF_V: track 65.6 -> 0.00 mm, vias 2 -> 0
- net MOTOR1_PWM_UH: track 63.4 -> 0.00 mm, vias 2 -> 0
- net VBUS_SENSE: track 62.9 -> 0.00 mm, vias 3 -> 0
- net MOTOR2_PWM_VL: track 62.5 -> 0.00 mm, vias 2 -> 0
- net MOTOR2_PWM_UL: track 60.1 -> 0.00 mm, vias 2 -> 0
- net SERVO1_PWM_X: track 59.2 -> 0.00 mm, vias 1 -> 0
- net MOTOR2_BEMF_U: track 58.8 -> 0.00 mm, vias 2 -> 0
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- removed copper zone on In1.Cu, net +3.3V
- removed copper zone on F.Cu, net +5V
- removed copper zone on F.Cu, net /power/BATTERY_IN
- removed copper zone on B.Cu, net GND
- removed copper zone on F.Cu, net GND
- removed copper zone on In1.Cu, net GND
- removed copper zone on In2.Cu, net GND
- removed copper zone on F.Cu, net Net-(D3-K)
- removed copper zone on F.Cu, net VBUS
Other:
- board size 100 x 70 mm -> 100 x 60 mm
- board text removed: "-"
- board text removed: "5V"
- board text removed: "ADC"
- board text removed: "BATTERY"
- board text removed: "CMP"
- board text removed: "ESP EN ESP BOOT"
- board text removed: "ESP LED"
- board text removed: "G"
- board text removed: "MOTOR 1"
- board text removed: "MOTOR 2"
- board text removed: "PWM"
- board text removed: "S"
- board text removed: "SERVO1"
- board text removed: "SERVO2"
- board text removed: "STM LED"
- board text removed: "STM RST"
- board text removed: "U"
- board text removed: "USB"
- board text removed: "V"
- board text removed: "W"
